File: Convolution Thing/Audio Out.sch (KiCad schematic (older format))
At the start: 27 parts

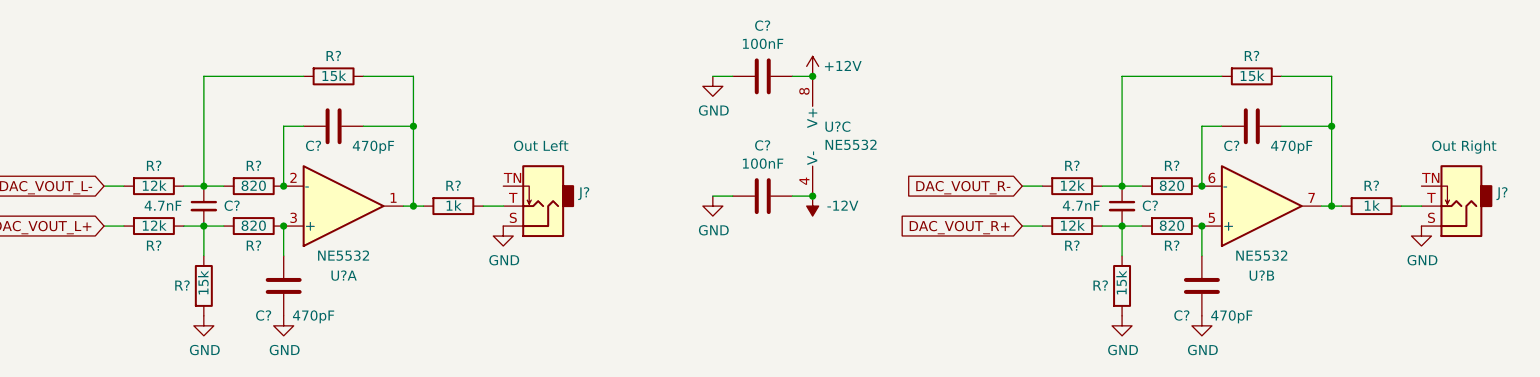
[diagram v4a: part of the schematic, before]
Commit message: Fix some issues, add component references
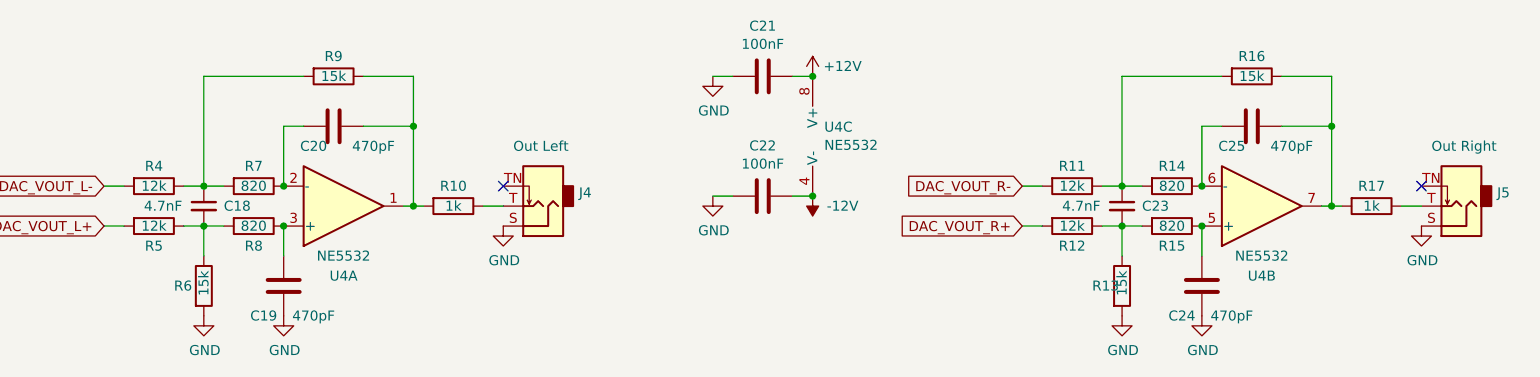
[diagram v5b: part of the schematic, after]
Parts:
- gave numbers to parts that had none: 25
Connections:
- no-connect marks 0 -> 2
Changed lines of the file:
@@
 $EndDescr
 $Comp
-L Amplifier_Operational:NE5532 U?
+L Amplifier_Operational:NE5532 U4
 U 1 1 611A2328
 P 2350 1650
-F 0 "U?" H 2350 2000 50  0000 C CNN
+F 0 "U4" H 2350 2000 50  0000 C CNN
 F 1 "NE5532" H 2350 1900 50  0000 C CNN
 F 2 "" H 2350 1650 50  0001 C CNN
@@
 $EndComp
 $Comp
-L Device:R R?
+L Device:R R7
 U 1 1 611B0B20
 P 1900 1550
-F 0 "R?" V 1800 1550 50  0000 C CNN
+F 0 "R7" V 1800 1550 50  0000 C CNN
 F 1 "820" V 1900 1550 50  0000 C CNN
 F 2 "" V 1830 1550 50  0001 C CNN
@@
 Connection ~ 1650 1550
 $Comp
-L Device:C_Small C?
+L Device:C_Small C18
 U 1 1 611B450A
 P 1650 1650
-F 0 "C?" H 1750 1650 50  0000 L CNN
+F 0 "C18" H 1750 1650 50  0000 L CNN
 F 1 "4.7nF" H 1350 1650 50  0000 L CNN
 F 2 "" H 1650 1650 50  0001 C CNN
@@
 $EndComp
 $Comp
-L Device:R R?
+L Device:R R8
 U 1 1 611B5FEA
 P 1900 1750
-F 0 "R?" V 2000 1750 50  0000 C CNN
+F 0 "R8" V 2000 1750 50  0000 C CNN
 F 1 "820" V 1900 1750 50  0000 C CNN
 F 2 "" V 1830 1750 50  0001 C CNN
@@
 Connection ~ 1650 1750
 $Comp
-L power:GND #PWR?
+L power:GND #PWR041
 U 1 1 611B9F73
 P 1650 2200
-F 0 "#PWR?" H 1650 1950 50  0001 C CNN
+F 0 "#PWR041" H 1650 1950 50  0001 C CNN
 F 1 "GND" H 1655 2027 50  0000 C CNN
 F 2 "" H 1650 2200 50  0001 C CNN
@@
 	1650 1900 1650 1750
 $Comp
-L Device:C C?
+L Device:C C19
 U 1 1 611BBD64
 P 2050 2050
-F 0 "C?" H 2150 2200 50  0000 C CNN
+F 0 "C19" H 2150 2200 50  0000 C CNN
 F 1 "470pF" H 1900 2200 50  0000 C CNN
 F 2 "" H 2088 1900 50  0001 C CNN
@@
 $EndComp
 $Comp
-L power:GND #PWR?
+L power:GND #PWR042
 U 1 1 611BC324
 P 2050 2200
-F 0 "#PWR?" H 2050 1950 50  0001 C CNN
+F 0 "#PWR042" H 2050 1950 50  0001 C CNN
 F 1 "GND" H 2055 2027 50  0000 C CNN
 F 2 "" H 2050 2200 50  0001 C CNN
@@
 Connection ~ 2050 1750
 $Comp
-L Device:R R?
+L Device:R R10
 U 1 1 611BE2CB
 P 2900 1650
-F 0 "R?" V 2800 1650 50  0000 C CNN
+F 0 "R10" V 2800 1650 50  0000 C CNN
 F 1 "1k" V 2900 1650 50  0000 C CNN
 F 2 "" V 2830 1650 50  0001 C CNN
@@
 	3150 1650 3050 1650
 $Comp
-L power:GND #PWR?
+L power:GND #PWR043
 U 1 1 611C0D52
 P 3150 1750
-F 0 "#PWR?" H 3150 1500 50  0001 C CNN
+F 0 "#PWR043" H 3150 1500 50  0001 C CNN
 F 1 "GND" H 3155 1577 50  0000 C CNN
 F 2 "" H 3150 1750 50  0001 C CNN
@@
 $EndComp
 $Comp
-L Amplifier_Operational:NE5532 U?
+L Amplifier_Operational:NE5532 U4
 U 3 1 611D5C9C
 P 4800 1300
-F 0 "U?" H 4758 1346 50  0000 L CNN
+F 0 "U4" H 4758 1346 50  0000 L CNN
 F 1 "NE5532" H 4758 1255 50  0000 L CNN
 F 2 "" H 4800 1300 50  0001 C CNN
@@
 $EndComp
 $Comp
-L power:+12V #PWR?
+L power:+12V #PWR046
 U 1 1 611D5CA2
 P 4700 1000
-F 0 "#PWR?" H 4700 850 50  0001 C CNN
+F 0 "#PWR046" H 4700 850 50  0001 C CNN
 F 1 "+12V" H 4850 1050 50  0000 C CNN
 F 2 "" H 4700 1000 50  0001 C CNN
@@
 $EndComp
 $Comp
-L power:-12V #PWR?
+L power:-12V #PWR047
 U 1 1 611D5CA8
 P 4700 1600
-F 0 "#PWR?" H 4700 1700 50  0001 C CNN
+F 0 "#PWR047" H 4700 1700 50  0001 C CNN
 F 1 "-12V" H 4550 1650 50  0000 C CNN
 F 2 "" H 4700 1600 50  0001 C CNN
@@
 Connection ~ 4700 1000
 $Comp
-L Device:C C?
+L Device:C C22
 U 1 1 611D5CAF
 P 4450 1600
-F 0 "C?" V 4198 1600 50  0000 C CNN
+F 0 "C22" V 4198 1600 50  0000 C CNN
 F 1 "100nF" V 4289 1600 50  0000 C CNN
 F 2 "" H 4488 1450 50  0001 C CNN
@@
 $EndComp
 $Comp
-L power:GND #PWR?
+L power:GND #PWR045
 U 1 1 611D5CB5
 P 4200 1600
-F 0 "#PWR?" H 4200 1350 50  0001 C CNN
+F 0 "#PWR045" H 4200 1350 50  0001 C CNN
 F 1 "GND" H 4205 1427 50  0000 C CNN
 F 2 "" H 4200 1600 50  0001 C CNN
@@
 Connection ~ 4700 1600
 $Comp
-L Device:C C?
+L Device:C C21
 U 1 1 611D5CBC
 P 4450 1000
-F 0 "C?" V 4198 1000 50  0000 C CNN
+F 0 "C21" V 4198 1000 50  0000 C CNN
 F 1 "100nF" V 4289 1000 50  0000 C CNN
 F 2 "" H 4488 850 50  0001 C CNN
@@
 $EndComp
 $Comp
-L power:GND #PWR?
+L power:GND #PWR044
 U 1 1 611D5CC2
 P 4200 1000
-F 0 "#PWR?" H 4200 750 50  0001 C CNN
+F 0 "#PWR044" H 4200 750 50  0001 C CNN
 F 1 "GND" H 4205 827 50  0000 C CNN
 F 2 "" H 4200 1000 50  0001 C CNN
@@
 DAC_VOUT_L-
 $Comp
-L Device:R R?
+L Device:R R6
 U 1 1 611B99F9
 P 1650 2050
-F 0 "R?" H 1500 2050 50  0000 L CNN
+F 0 "R6" H 1500 2050 50  0000 L CNN
 F 1 "15k" V 1650 2000 50  0000 L CNN
 F 2 "" V 1580 2050 50  0001 C CNN
@@
 $EndComp
 $Comp
-L Device:R R?
+L Device:R R5
 U 1 1 611B6DC9
 P 1400 1750
-F 0 "R?" V 1500 1750 50  0000 C CNN
+F 0 "R5" V 1500 1750 50  0000 C CNN
 F 1 "12k" V 1400 1750 50  0000 C CNN
 F 2 "" V 1330 1750 50  0001 C CNN
@@
 $EndComp
 $Comp
-L Device:R R?
+L Device:R R9
 U 1 1 611AFAE7
 P 2300 1000
-F 0 "R?" V 2200 1000 50  0000 C CNN
+F 0 "R9" V 2200 1000 50  0000 C CNN
 F 1 "15k" V 2300 1000 50  0000 C CNN
 F 2 "" V 2230 1000 50  0001 C CNN
@@
 $EndComp
 $Comp
-L Device:R R?
+L Device:R R4
 U 1 1 611A9639
 P 1400 1550
-F 0 "R?" V 1300 1550 50  0000 C CNN
+F 0 "R4" V 1300 1550 50  0000 C CNN
 F 1 "12k" V 1400 1550 50  0000 C CNN
 F 2 "" V 1330 1550 50  0001 C CNN
@@
 	2700 1250 2700 1650
 $Comp
-L Device:C C?
+L Device:C C20
 U 1 1 611B100B
 P 2300 1250
-F 0 "C?" V 2400 1150 50  0000 C CNN
+F 0 "C20" V 2400 1150 50  0000 C CNN
 F 1 "470pF" V 2400 1450 50  0000 C CNN
 F 2 "" H 2338 1100 50  0001 C CNN
@@
 $EndComp
 $Comp
-L Amplifier_Operational:NE5532 U?
+L Amplifier_Operational:NE5532 U4
 U 2 1 610EFD35
 P 6950 1650
-F 0 "U?" H 6950 2000 50  0000 C CNN
+F 0 "U4" H 6950 2000 50  0000 C CNN
 F 1 "NE5532" H 6950 1900 50  0000 C CNN
 F 2 "" H 6950 1650 50  0001 C CNN
@@
 $EndComp
 $Comp
-L Device:R R?
+L Device:R R14
 U 1 1 610EFD3B
 P 6500 1550
-F 0 "R?" V 6400 1550 50  0000 C CNN
+F 0 "R14" V 6400 1550 50  0000 C CNN
 F 1 "820" V 6500 1550 50  0000 C CNN
 F 2 "" V 6430 1550 50  0001 C CNN
@@
 Connection ~ 6250 1550
 $Comp
-L Device:C_Small C?
+L Device:C_Small C23
 U 1 1 610EFD45
 P 6250 1650
-F 0 "C?" H 6350 1650 50  0000 L CNN
+F 0 "C23" H 6350 1650 50  0000 L CNN
 F 1 "4.7nF" H 5950 1650 50  0000 L CNN
 F 2 "" H 6250 1650 50  0001 C CNN
@@
 $EndComp
 $Comp
-L Device:R R?
+L Device:R R15
 U 1 1 610EFD4B
 P 6500 1750
-F 0 "R?" V 6600 1750 50  0000 C CNN
+F 0 "R15" V 6600 1750 50  0000 C CNN
 F 1 "820" V 6500 1750 50  0000 C CNN
 F 2 "" V 6430 1750 50  0001 C CNN
@@
 Connection ~ 6250 1750
 $Comp
-L power:GND #PWR?
+L power:GND #PWR048
 U 1 1 610EFD52
 P 6250 2200
-F 0 "#PWR?" H 6250 1950 50  0001 C CNN
+F 0 "#PWR048" H 6250 1950 50  0001 C CNN
 F 1 "GND" H 6255 2027 50  0000 C CNN
 F 2 "" H 6250 2200 50  0001 C CNN
@@
 	6250 1900 6250 1750
 $Comp
-L Device:C C?
+L Device:C C24
 U 1 1 610EFD59
 P 6650 2050
-F 0 "C?" H 6750 2200 50  0000 C CNN
+F 0 "C24" H 6750 2200 50  0000 C CNN
 F 1 "470pF" H 6500 2200 50  0000 C CNN
 F 2 "" H 6688 1900 50  0001 C CNN
@@
 $EndComp
 $Comp
-L power:GND #PWR?
+L power:GND #PWR049
 U 1 1 610EFD5F
 P 6650 2200
-F 0 "#PWR?" H 6650 1950 50  0001 C CNN
+F 0 "#PWR049" H 6650 1950 50  0001 C CNN
 F 1 "GND" H 6655 2027 50  0000 C CNN
 F 2 "" H 6650 2200 50  0001 C CNN
@@
 Connection ~ 6650 1750
 $Comp
-L Device:R R?
+L Device:R R17
 U 1 1 610EFD67
 P 7500 1650
-F 0 "R?" V 7400 1650 50  0000 C CNN
+F 0 "R17" V 7400 1650 50  0000 C CNN
 F 1 "1k" V 7500 1650 50  0000 C CNN
 F 2 "" V 7430 1650 50  0001 C CNN
@@
 	7750 1650 7650 1650
 $Comp
-L power:GND #PWR?
+L power:GND #PWR050
 U 1 1 610EFD74
 P 7750 1750
-F 0 "#PWR?" H 7750 1500 50  0001 C CNN
+F 0 "#PWR050" H 7750 1500 50  0001 C CNN
 F 1 "GND" H 7755 1577 50  0000 C CNN
 F 2 "" H 7750 1750 50  0001 C CNN
@@
 DAC_VOUT_R-
 $Comp
-L Device:R R?
+L Device:R R13
 U 1 1 610EFD7C
 P 6250 2050
-F 0 "R?" H 6100 2050 50  0000 L CNN
+F 0 "R13" H 6100 2050 50  0000 L CNN
 F 1 "15k" V 6250 2000 50  0000 L CNN
 F 2 "" V 6180 2050 50  0001 C CNN
@@
 $EndComp
 $Comp
-L Device:R R?
+L Device:R R12
 U 1 1 610EFD82
 P 6000 1750
-F 0 "R?" V 6100 1750 50  0000 C CNN
+F 0 "R12" V 6100 1750 50  0000 C CNN
 F 1 "12k" V 6000 1750 50  0000 C CNN
 F 2 "" V 5930 1750 50  0001 C CNN
@@
 $EndComp
 $Comp
-L Device:R R?
+L Device:R R16
 U 1 1 610EFD88
 P 6900 1000
-F 0 "R?" V 6800 1000 50  0000 C CNN
+F 0 "R16" V 6800 1000 50  0000 C CNN
 F 1 "15k" V 6900 1000 50  0000 C CNN
 F 2 "" V 6830 1000 50  0001 C CNN
@@
 $EndComp
 $Comp
-L Device:R R?
+L Device:R R11
 U 1 1 610EFD8E
 P 6000 1550
-F 0 "R?" V 5900 1550 50  0000 C CNN
+F 0 "R11" V 5900 1550 50  0000 C CNN
 F 1 "12k" V 6000 1550 50  0000 C CNN
 F 2 "" V 5930 1550 50  0001 C CNN
@@
 	7300 1250 7300 1650
 $Comp
-L Device:C C?
+L Device:C C25
 U 1 1 610EFDA4
 P 6900 1250
-F 0 "C?" V 7000 1150 50  0000 C CNN
+F 0 "C25" V 7000 1150 50  0000 C CNN
 F 1 "470pF" V 7000 1450 50  0000 C CNN
 F 2 "" H 6938 1100 50  0001 C CNN
@@
 P 3350 1650
 AR Path="/61055545/610C7132" Ref="J?"  Part="1"
-AR Path="/610554DD/610C7132" Ref="J?"  Part="1"
-F 0 "J?" H 3171 1583 50  0000 R CNN
+AR Path="/610554DD/610C7132" Ref="J4"  Part="1"
+F 0 "J4" H 3171 1583 50  0000 R CNN
 F 1 "Out Left" H 3500 1350 50  0000 R CNN
 F 2 "" H 3350 1650 50  0001 C CNN
@@
 P 7950 1650
 AR Path="/61055545/610C7D48" Ref="J?"  Part="1"
-AR Path="/610554DD/610C7D48" Ref="J?"  Part="1"
-F 0 "J?" H 7771 1583 50  0000 R CNN
+AR Path="/610554DD/610C7D48" Ref="J5"  Part="1"
+F 0 "J5" H 7771 1583 50  0000 R CNN
 F 1 "Out Right" H 8100 1350 50  0000 R CNN
 F 2 "" H 7950 1650 50  0001 C CNN
@@
 	-1   0    0    1
 $EndComp
+NoConn ~ 3150 1550
+NoConn ~ 7750 1550
 $EndSCHEMATC
